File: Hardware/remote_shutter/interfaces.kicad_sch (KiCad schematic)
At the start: 9 parts

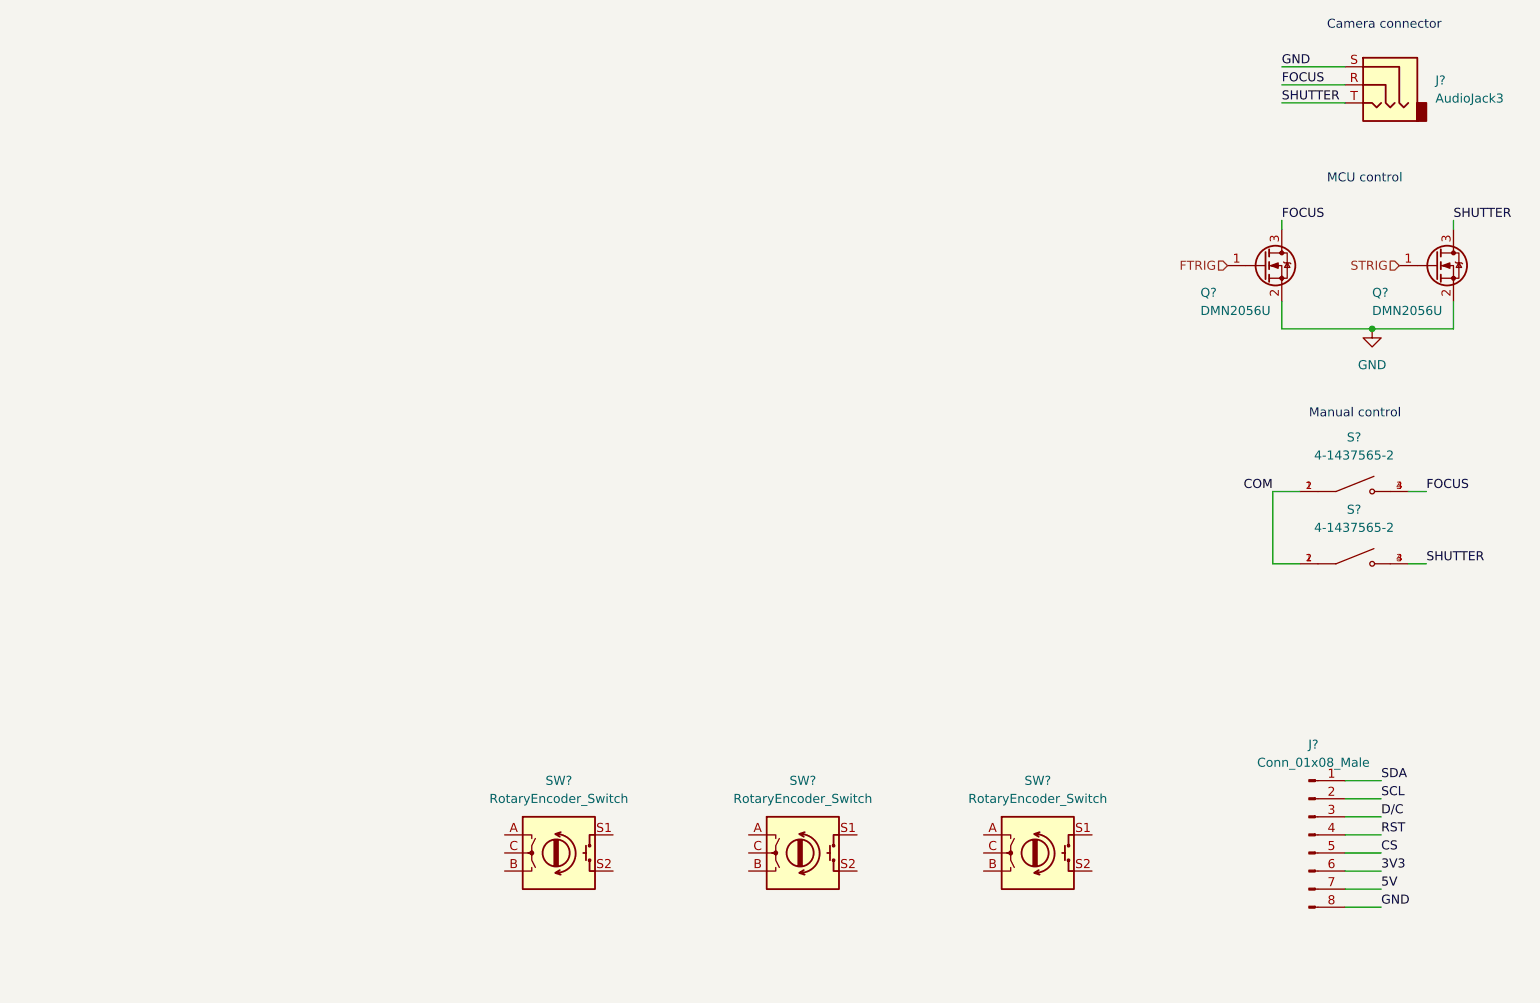
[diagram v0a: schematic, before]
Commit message: Added power & comms.
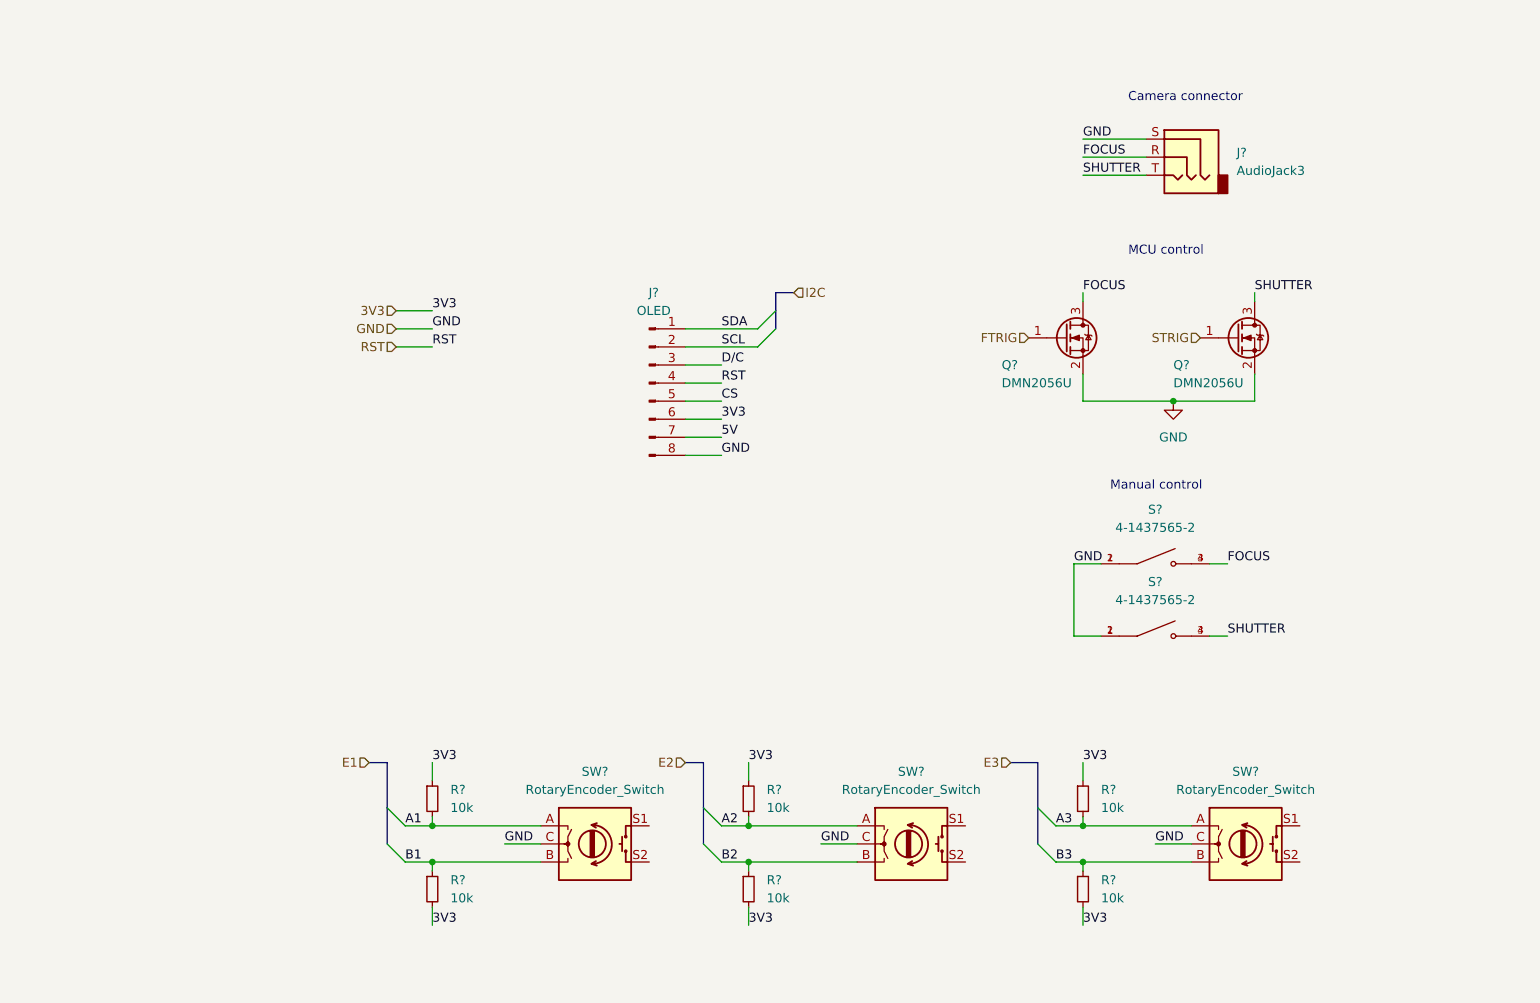
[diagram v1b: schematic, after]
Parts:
- removed SW? (x2): RotaryEncoder_Switch, symbol Device:RotaryEncoder_Switch
- added R? (x6): 10k, symbol Device:R_Small
- added SW? (x2): RotaryEncoder_Switch, symbol Device:RotaryEncoder_Switch
- J?: value Conn_01x08_Male -> OLED
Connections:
- net COM is gone; now on net GND: S?.1, S?.1, S?.2, S?.2
- net 3V3: now also R?.1, R?.1, R?.1, R?.2, R?.2, R?.2
- net GND: now also SW?.C, SW?.C, SW?.C
- net A1: now reaches SW?.A
- net A1: now also R?.2
- net B1: now reaches SW?.B
- net B1: now also R?.1
- new net A2: R?.2, SW?.A
- new net A3: R?.2, SW?.A
- new net B2: R?.1, SW?.B
- new net B3: R?.1, SW?.B
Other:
- moved on the sheet: J?, Q?, S?, SW?

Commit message: Added missing footprints. First PCB export.
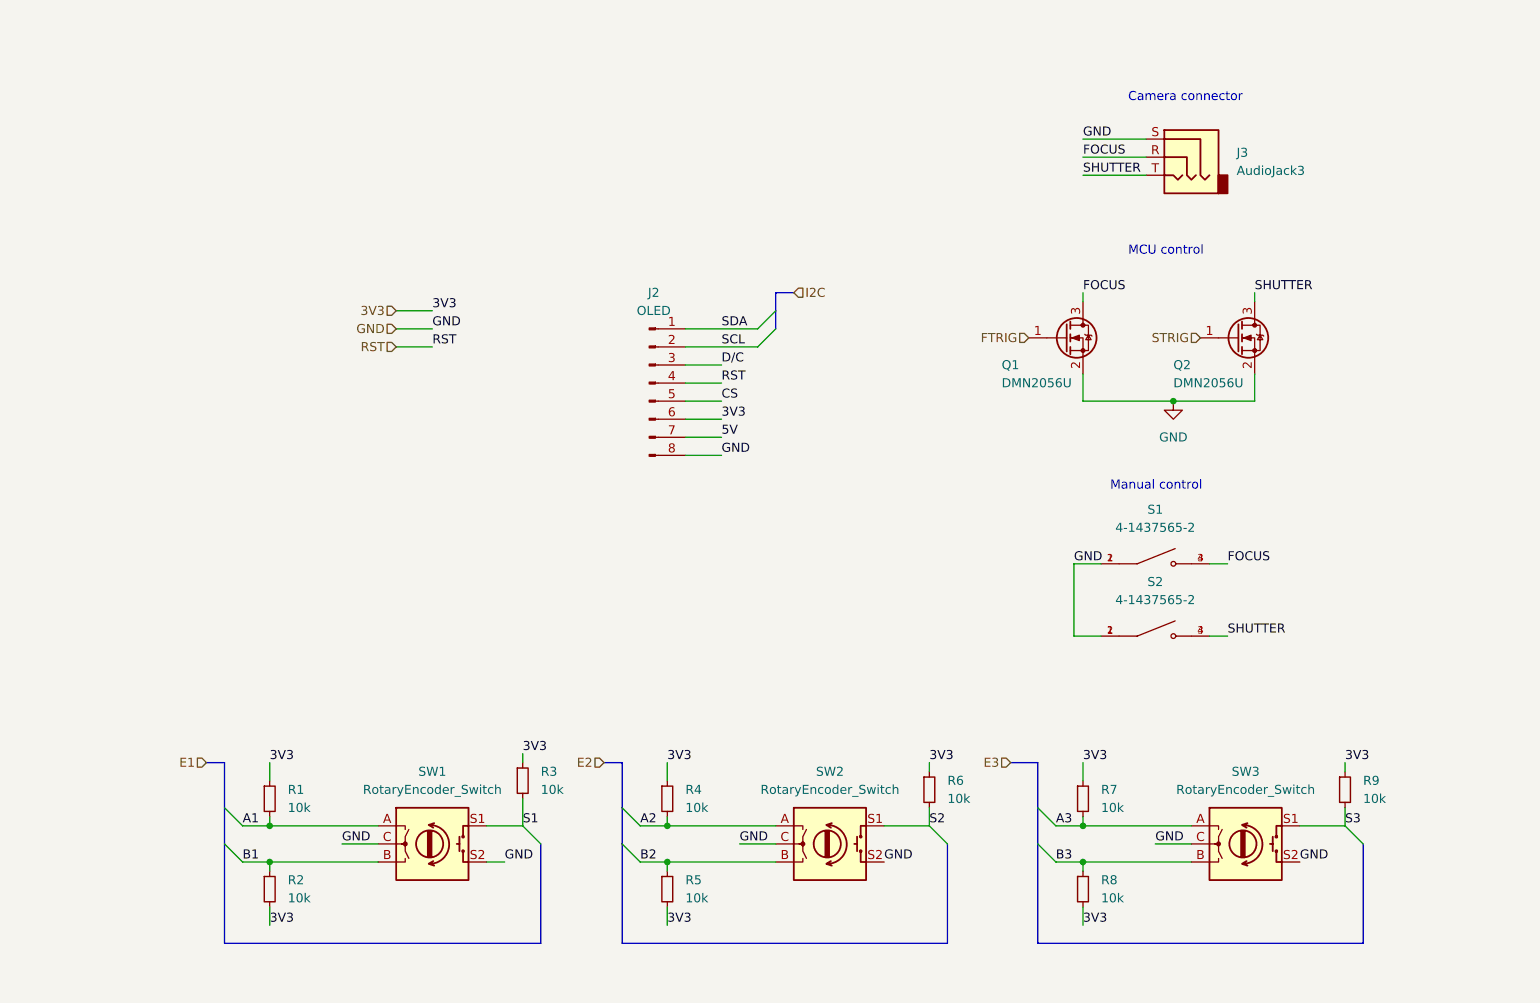
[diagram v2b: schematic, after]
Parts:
- added R3, R6, R9: 10k, Resistor_SMD:R_0603_1608Metric_Pad0.98x0.95mm_HandSolder, symbol Device:R_Small
- J3: renamed from J?; footprint (none) -> footprint:PJ-320B
- R1, R2, R4, R5, R7, R8: renamed from R?; footprint (none) -> Resistor_SMD:R_0603_1608Metric_Pad0.98x0.95mm_HandSolder
- S1, S2: renamed from S?; footprint SW_4-1437565-2 -> footprint:SW_4-1437565-2
- SW1, SW2, SW3: renamed from SW?; footprint (none) -> footprint:PEC16
- gave numbers to parts that had none: 3
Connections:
- net 3V3: now also R3.1, R6.1, R9.1
- net GND: now also SW1.S2, SW2.S2, SW3.S2
- net S2: now reaches SW2.S1
- net S2: now also R6.2
- net S3: now reaches SW3.S1
- net S3: now also R9.2
- net S1: now reaches SW1.S1
- net S1: now also R3.2
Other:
- moved on the sheet: R1, R2, R4, R5, SW1, SW2

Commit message: Fixed bus routing
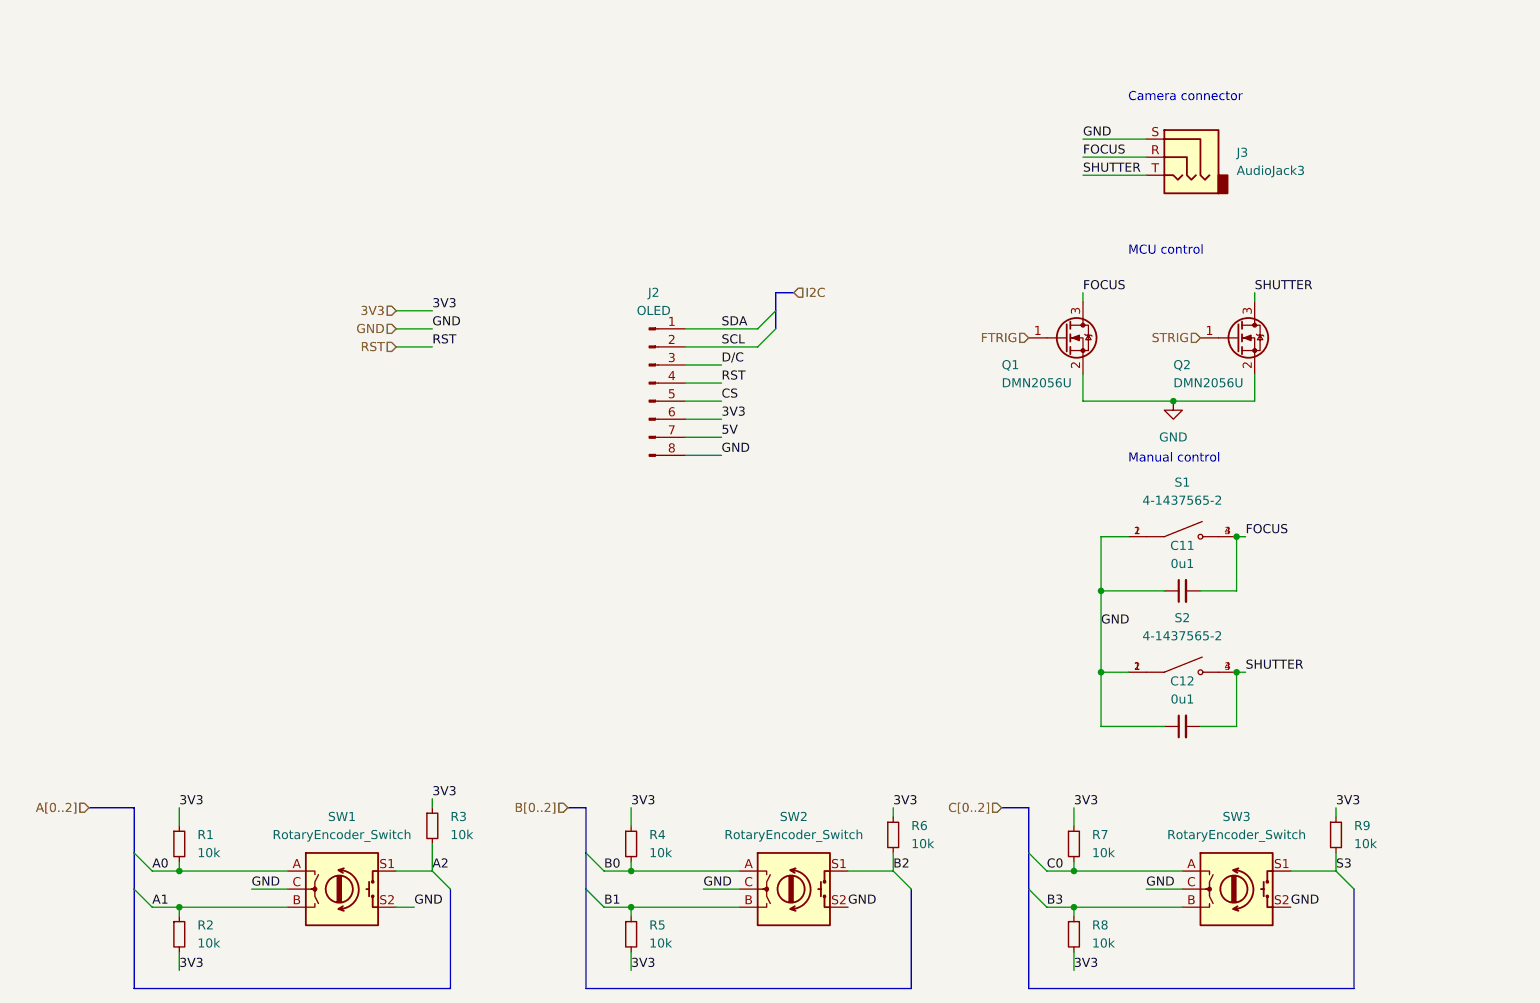
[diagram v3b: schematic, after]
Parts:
- added C11, C12: 0u1, Capacitor_SMD:C_0603_1608Metric_Pad1.08x0.95mm_HandSolder, symbol Device:C_Small
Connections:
- net S1 is gone; now on net A2: R3.2, SW1.S1
- net S2 is gone; now on net B2: R6.2, SW2.S1
- net A1: now also R2.1, SW1.B; no longer R1.2, SW1.A
- net A2: no longer R4.2, SW2.A
- net B1: now also R5.1, SW2.B; no longer R2.1, SW1.B
- net B2: no longer R5.1, SW2.B
- net FOCUS: now also C11.2
- net GND: now also C11.1, C12.1
- net SHUTTER: now also C12.2
- net A3 renamed C0
- new net A0: R1.2, SW1.A
- new net B0: R4.2, SW2.A
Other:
- moved on the sheet: R1, R2, R3, R4, R5, R6, R7, R8, R9, S1, S2, SW1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

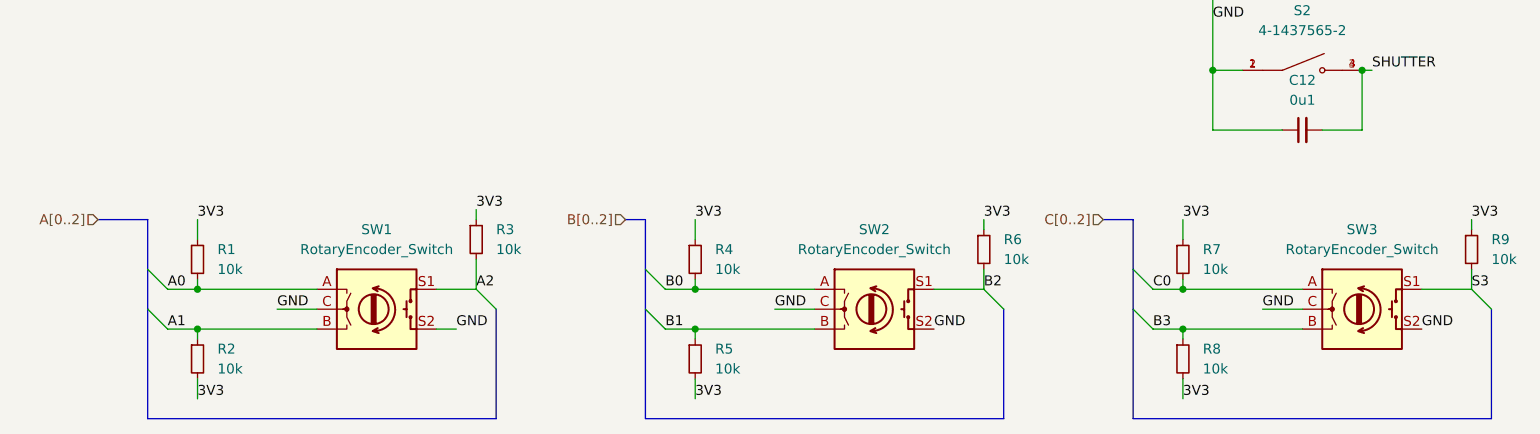
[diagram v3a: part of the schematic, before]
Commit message: Replaced rotary encoders
Now one flat to save space.
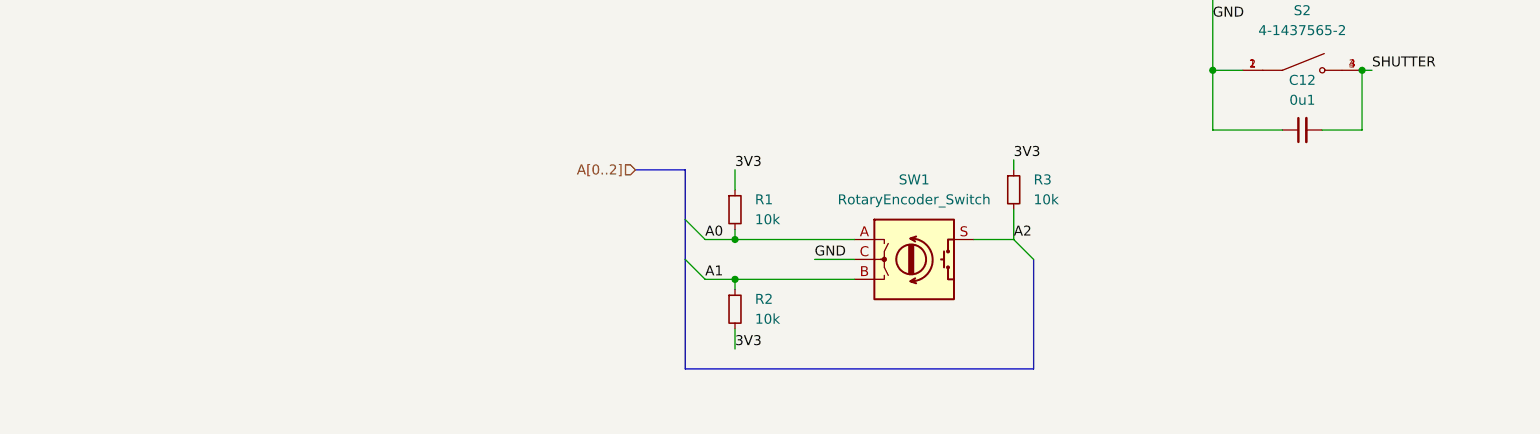
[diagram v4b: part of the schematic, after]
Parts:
- removed R4, R5, R6, R7, R8, R9: 10k, Resistor_SMD:R_0603_1608Metric_Pad0.98x0.95mm_HandSolder, symbol Device:R_Small
- removed SW2, SW3: RotaryEncoder_Switch, footprint:PEC16, symbol Device:RotaryEncoder_Switch
- SW1: footprint footprint:PEC16 -> footprint:SIQ-02FVS3
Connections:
- net A2: now also SW1.S; no longer SW1.S1
- net GND: no longer SW1.S2
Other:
- moved on the sheet: R1, R2, R3

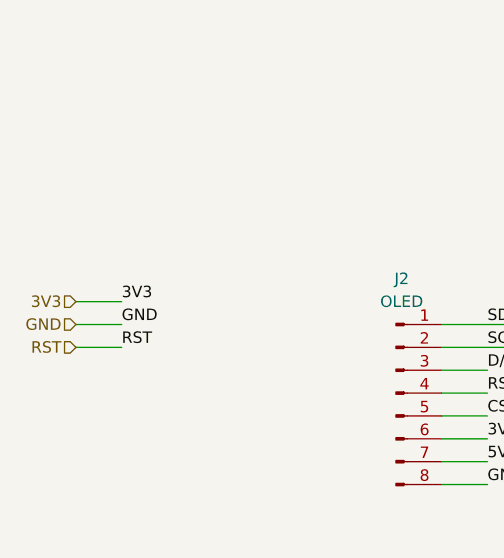
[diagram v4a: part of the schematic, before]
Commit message: Started routing. Added power switch.
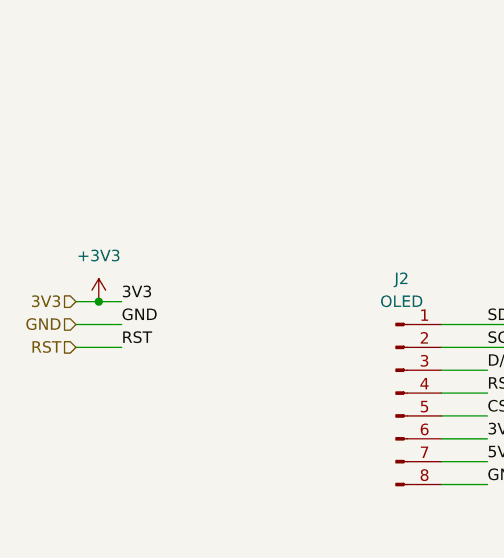
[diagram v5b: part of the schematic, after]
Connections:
- net 3V3 renamed +3V3
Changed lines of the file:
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@@
 (kicad_sch (version 20211123) (generator eeschema)
   (paper "A4")
+  (junction (at 78.74 68.58) (diameter 0) (color 0 0 0 0)
+  )
   (junction (at 194.31 119.38) (diameter 0) (color 0 0 0 0)
   )
@@
     (stroke (width 0) (type default) (color 0 0 0 0))
   )
+  (wire (pts (xy 78.74 68.58) (xy 81.28 68.58))
+    (stroke (width 0) (type default) (color 0 0 0 0))
+  )
   (wire (pts (xy 149.86 130.81) (xy 149.86 132.08))
     (stroke (width 0) (type default) (color 0 0 0 0))
@@
     (stroke (width 0) (type default) (color 0 0 0 0))
   )
-  (wire (pts (xy 76.2 68.58) (xy 81.28 68.58))
+  (wire (pts (xy 76.2 68.58) (xy 78.74 68.58))
     (stroke (width 0) (type default) (color 0 0 0 0))
   )
@@
     (pin "2")
   )
+  (symbol (lib_id "power:+3V3") (at 78.74 68.58 0) (unit 1)
+    (in_bom yes) (on_board yes) (fields_autoplaced)
+    (property "Reference" "#PWR?" (id 0) (at 78.74 72.39 0)
+      (effects (font (size 1.27 1.27)) hide)
+    )
+    (property "Value" "+3V3" (id 1) (at 78.74 63.5 0))
+    (property "Footprint" "" (id 2) (at 78.74 68.58 0)
+      (effects (font (size 1.27 1.27)) hide)
+    )
+    (property "Datasheet" "" (id 3) (at 78.74 68.58 0)
+      (effects (font (size 1.27 1.27)) hide)
+    )
+    (pin "1")
+  )
   (symbol (lib_id "4-1437565-2:4-1437565-2") (at 186.69 119.38 0) (unit 1)
